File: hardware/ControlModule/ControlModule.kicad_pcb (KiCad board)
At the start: 2 copper layers, 100 x 50 mm, 25 parts, among them J1 ICSP, J10 Conn_01x02, J11 Conn_01x02, J2 Conn_01x03, J3 I2C/ICSP/UART, J4 Conn_01x06, J5 Conn_01x02, J6 Conn_01x02, J7 ICSP, J8 Conn_01x02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

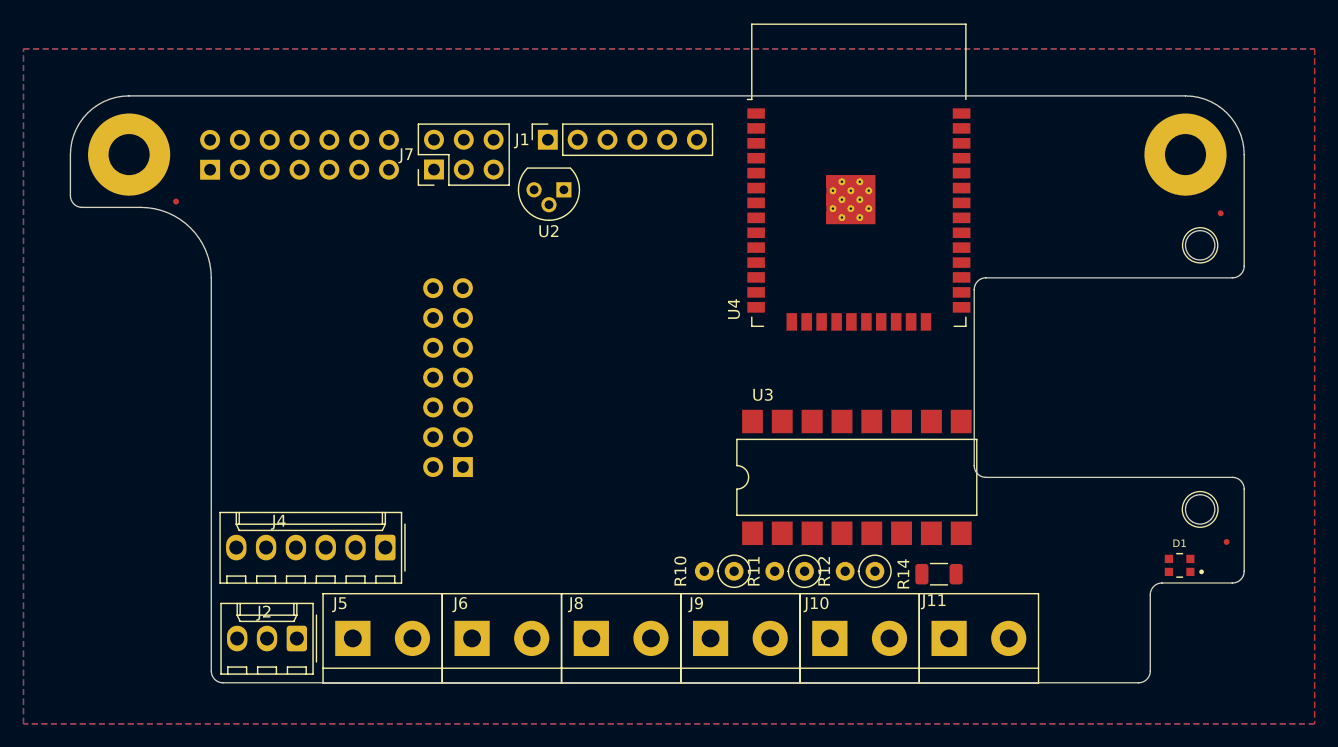
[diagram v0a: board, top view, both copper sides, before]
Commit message: add some new PCB's
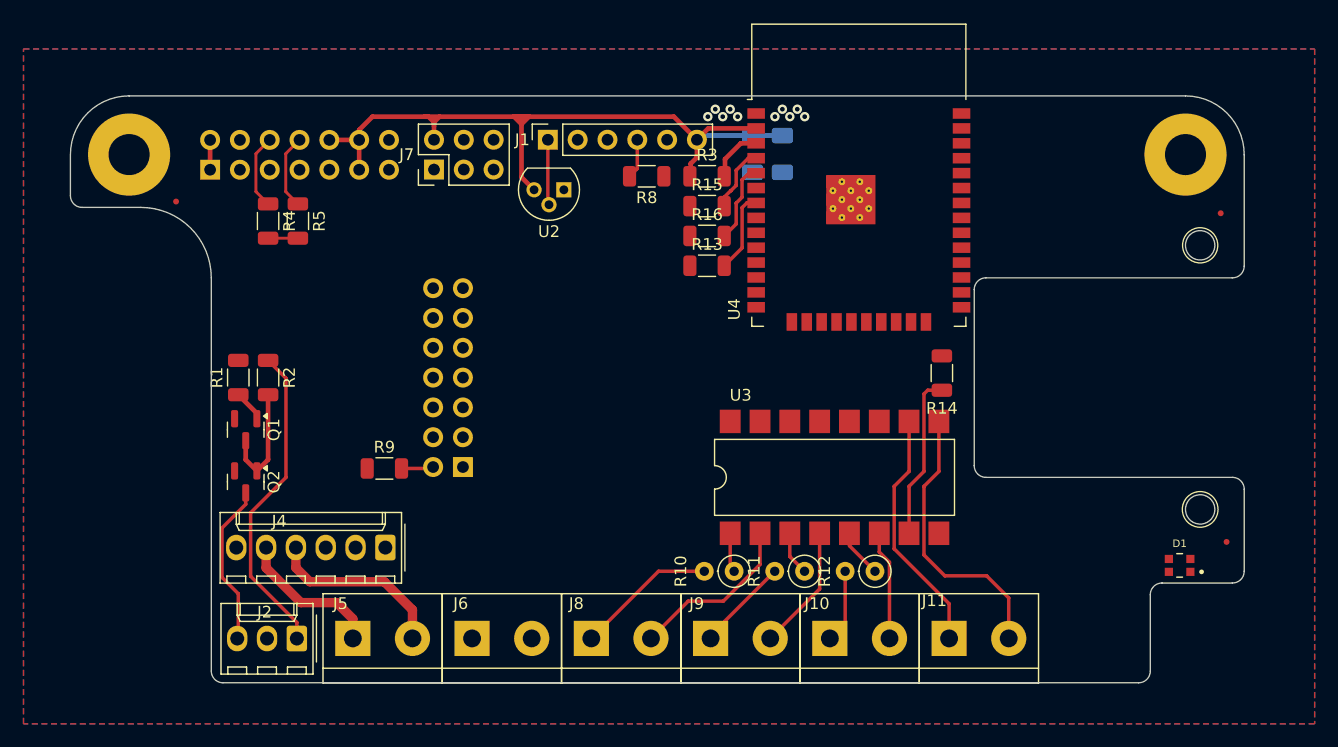
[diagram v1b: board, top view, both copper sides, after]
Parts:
- added C1: 100nF, Capacitor_SMD:C_1206_3216Metric_Pad1.33x1.80mm_HandSolder, B.Cu at (160.7, 67.9)
- added C2: 1uF, Capacitor_SMD:C_1206_3216Metric_Pad1.33x1.80mm_HandSolder, B.Cu at (158.1, 67.9)
- added Q1: BC817, Package_TO_SOT_SMD:SOT-23, F.Cu at (114.9, 91.4)
- added Q2: IRLML2502, Package_TO_SOT_SMD:SOT-23, F.Cu at (114.9, 95.9)
- added R1: 1k, Resistor_SMD:R_1206_3216Metric, F.Cu at (114.3, 87.0)
- added R13: 10k, Resistor_SMD:R_1206_3216Metric, F.Cu at (154.2, 77.5)
- added R15: 10k, Resistor_SMD:R_1206_3216Metric, F.Cu at (154.2, 72.4)
- added R16: 10k, Resistor_SMD:R_1206_3216Metric, F.Cu at (154.2, 74.9)
- added R2: 10k, Resistor_SMD:R_1206_3216Metric, F.Cu at (116.8, 87.0)
- added R3: 10k, Resistor_SMD:R_1206_3216Metric, F.Cu at (154.2, 69.8)
- added R4: 100k, Resistor_SMD:R_1206_3216Metric, F.Cu at (116.8, 73.7)
- added R5: 100k, Resistor_SMD:R_1206_3216Metric, F.Cu at (119.4, 73.7)
- added R8: 10k, Resistor_SMD:R_1206_3216Metric, F.Cu at (149.1, 69.8)
- added R9: 10k, Resistor_SMD:R_1206_3216Metric, F.Cu at (126.7, 94.7)
- moved R14 17.1 mm to (174.2, 86.6), turned to -90 degrees
- moved U3 1.90 mm to (165.1, 95.5)
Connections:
- J2 pad 1: +12V -> Net-(J2-Pin_1)
- J5 pad 1: +3V3 -> +5V
- J5 pad 2: +5V -> +3V3
- J6 pad 1: +12V -> GND
- U4 pad 2: +3.3V -> +3V3
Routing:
- net +3V3: track 0.00 -> 83.2 mm
- net Net-(J2-Pin_1): track 0.00 -> 27.2 mm
- net Net-(J11-Pin_2): track 0.00 -> 24.1 mm
- net Net-(J11-Pin_1): track 0.00 -> 20.9 mm
- net +5V: track 0.00 -> 15.1 mm
- net Net-(J8-Pin_2): track 0.00 -> 14.6 mm
- net Net-(R14-Pad2): track 0.00 -> 14.1 mm
- net Net-(J2-Pin_3): track 0.00 -> 13.9 mm
- net Net-(J8-Pin_1): track 0.00 -> 12.0 mm
- net Net-(J9-Pin_2): track 0.00 -> 10.7 mm
- net RESET: track 0.00 -> 10.2 mm
- net Net-(Q1-C): track 0.00 -> 9.85 mm
- net Net-(J10-Pin_2): track 0.00 -> 9.32 mm
- net Net-(J9-Pin_1): track 0.00 -> 7.98 mm
- net I0: track 0.00 -> 6.94 mm
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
